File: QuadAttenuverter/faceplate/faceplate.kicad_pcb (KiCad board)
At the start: 2 copper layers, 40.3 x 128.5 mm, 20 parts

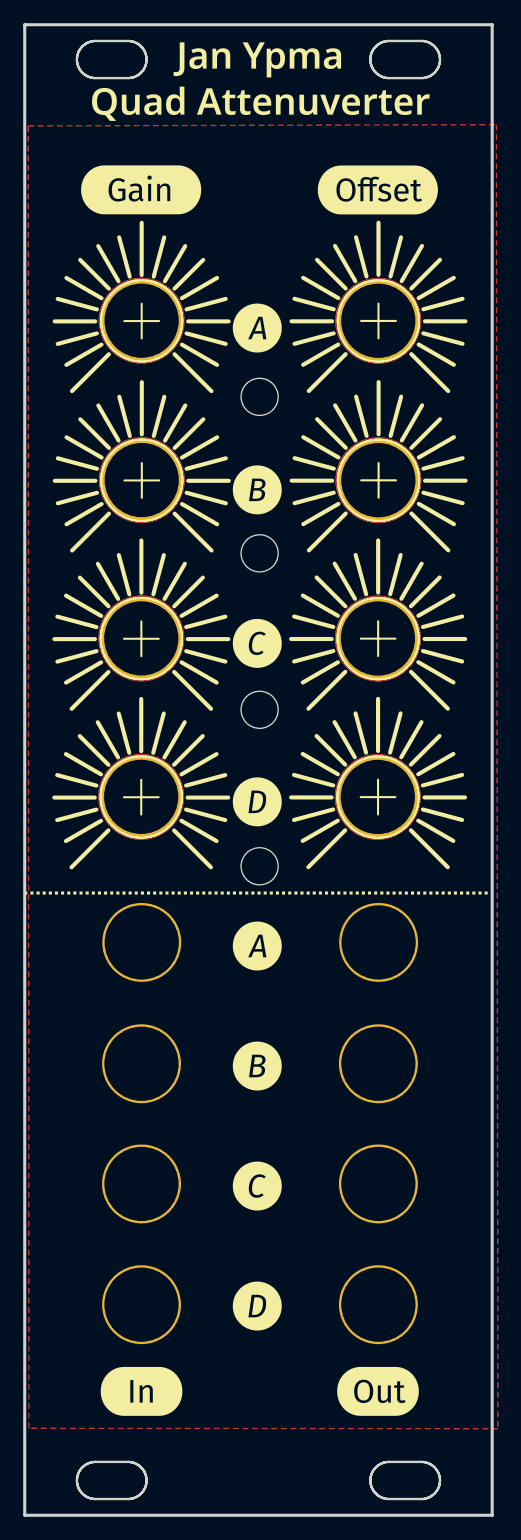
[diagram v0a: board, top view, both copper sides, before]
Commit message: Few faceplate cleanups to get rid of warnings
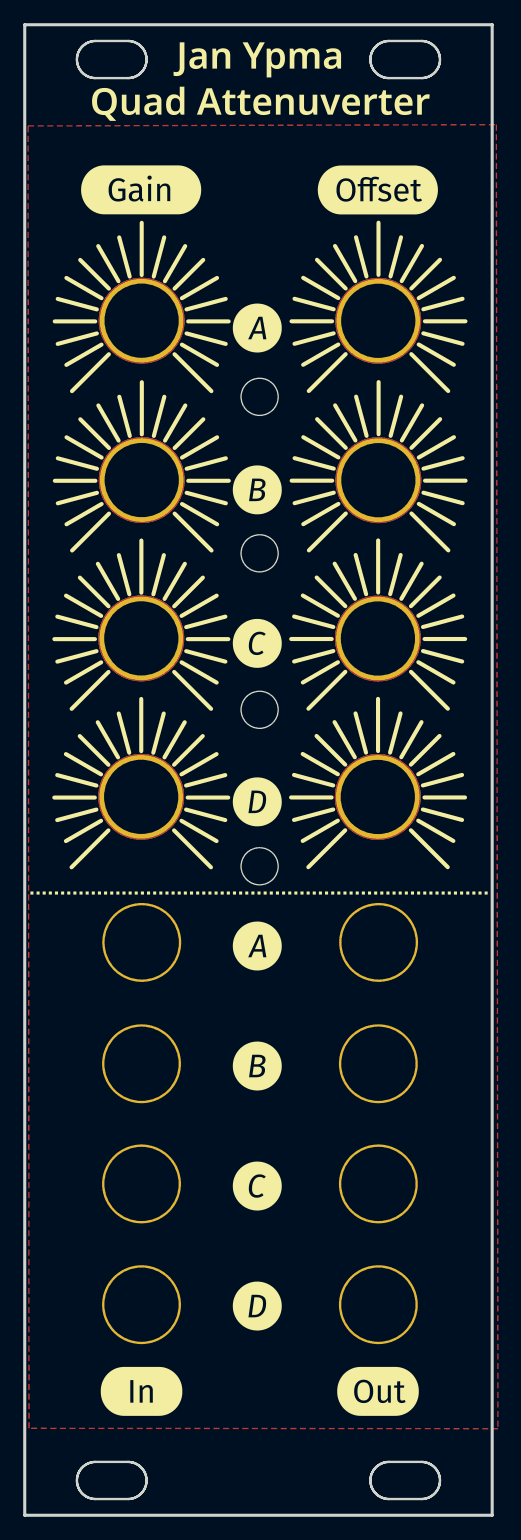
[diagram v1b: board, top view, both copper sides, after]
